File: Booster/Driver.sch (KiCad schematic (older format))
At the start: 5 parts

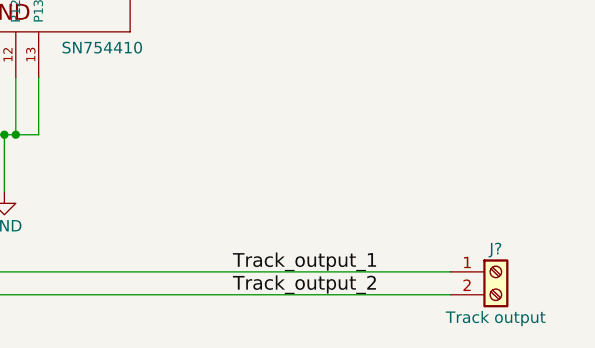
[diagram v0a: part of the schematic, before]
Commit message: First draft of detecting overcurrent.
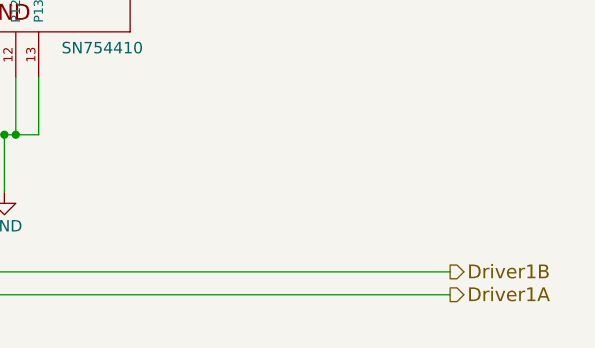
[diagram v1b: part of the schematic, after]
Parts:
- removed J?: Track output, symbol Screw_Terminal_01x02
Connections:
- net labels added: Driver1A, Driver1B
- net labels removed: Track_output_1, Track_output_2
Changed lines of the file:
@@
 $Descr A4 11693 8268
 encoding utf-8
-Sheet 4 4
+Sheet 4 5
 Title ""
 Date ""
@@
 Wire Wire Line
 	6500 5600 9150 5600
-$Comp
-L Screw_Terminal_01x02 J?
-U 1 1 59E91272
-P 9350 5500
-F 0 "J?" H 9350 5600 50  0000 C CNN
-F 1 "Track output" H 9350 5300 50  0000 C CNN
-F 2 "" H 9350 5500 50  0001 C CNN
-F 3 "" H 9350 5500 50  0001 C CNN
-	1    9350 5500
-	1    0    0    -1
-$EndComp
-Text Label 8200 5500 0    60   ~ 0
-Track_output_1
-Text Label 8200 5600 0    60   ~ 0
-Track_output_2
+Text HLabel 9150 5500 2    60   Output ~ 0
+Driver1B
+Text HLabel 9150 5600 2    60   Output ~ 0
+Driver1A
 $EndSCHEMATC

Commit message: Over current protection and detection - with detection delay and release delay.
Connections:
- net labels added: Enable_Driver, TrackA, TrackB, VCC_Driver
- net labels removed: +12V, DCC_Enable, Driver1A, Driver1B
- wire segments 29 -> 55
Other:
- moved on the sheet: C?
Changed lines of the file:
@@
-$EndComp
-$Comp
-L +12V #PWR?
-U 1 1 59E90E37
-P 7650 1900
-F 0 "#PWR?" H 7650 1750 50  0001 C CNN
-F 1 "+12V" H 7650 2040 50  0000 C CNN
-F 2 "" H 7650 1900 50  0001 C CNN
-F 3 "" H 7650 1900 50  0001 C CNN
-	1    7650 1900
-	1    0    0    -1
 $EndComp
 $Comp
 L C C?
 U 1 1 59E90E3D
-P 6950 2700
-F 0 "C?" H 6975 2800 50  0000 L CNN
-F 1 "100nF" H 6975 2600 50  0000 L CNN
-F 2 "" H 6988 2550 50  0001 C CNN
-F 3 "" H 6950 2700 50  0001 C CNN
-	1    6950 2700
+P 6950 2600
+F 0 "C?" H 6975 2700 50  0000 L CNN
+F 1 "100nF" H 6975 2500 50  0000 L CNN
+F 2 "" H 6988 2450 50  0001 C CNN
+F 3 "" H 6950 2600 50  0001 C CNN
+	1    6950 2600
 	1    0    0    -1
 $EndComp
@@
 L GND #PWR?
 U 1 1 59E90E44
-P 6950 3000
-F 0 "#PWR?" H 6950 2750 50  0001 C CNN
-F 1 "GND" H 6950 2850 50  0000 C CNN
-F 2 "" H 6950 3000 50  0001 C CNN
-F 3 "" H 6950 3000 50  0001 C CNN
-	1    6950 3000
+P 6950 2900
+F 0 "#PWR?" H 6950 2650 50  0001 C CNN
+F 1 "GND" H 6950 2750 50  0000 C CNN
+F 2 "" H 6950 2900 50  0001 C CNN
+F 3 "" H 6950 2900 50  0001 C CNN
+	1    6950 2900
 	1    0    0    -1
 $EndComp
@@
 L C C?
 U 1 1 59E90E4A
-P 7650 2700
-F 0 "C?" H 7675 2800 50  0000 L CNN
-F 1 "100nF" H 7675 2600 50  0000 L CNN
-F 2 "" H 7688 2550 50  0001 C CNN
-F 3 "" H 7650 2700 50  0001 C CNN
-	1    7650 2700
+P 7650 2600
+F 0 "C?" H 7675 2700 50  0000 L CNN
+F 1 "100nF" H 7675 2500 50  0000 L CNN
+F 2 "" H 7688 2450 50  0001 C CNN
+F 3 "" H 7650 2600 50  0001 C CNN
+	1    7650 2600
 	1    0    0    -1
 $EndComp
@@
 L GND #PWR?
 U 1 1 59E90E51
-P 7650 3000
-F 0 "#PWR?" H 7650 2750 50  0001 C CNN
-F 1 "GND" H 7650 2850 50  0000 C CNN
-F 2 "" H 7650 3000 50  0001 C CNN
-F 3 "" H 7650 3000 50  0001 C CNN
-	1    7650 3000
-	1    0    0    -1
-$EndComp
-Wire Wire Line
-	6950 1900 6950 2550
-Connection ~ 6950 2450
-Wire Wire Line
-	6950 3000 6950 2850
-Wire Wire Line
-	7650 3000 7650 2850
-Wire Wire Line
-	7650 1900 7650 2550
-Wire Wire Line
-	7650 2450 7350 2450
+P 7650 2900
+F 0 "#PWR?" H 7650 2650 50  0001 C CNN
+F 1 "GND" H 7650 2750 50  0000 C CNN
+F 2 "" H 7650 2900 50  0001 C CNN
+F 3 "" H 7650 2900 50  0001 C CNN
+	1    7650 2900
+	1    0    0    -1
+$EndComp
+Wire Wire Line
+	6950 1800 6950 2350
+Wire Wire Line
+	6950 2350 6950 2450
+Connection ~ 6950 2350
+Wire Wire Line
+	6950 2900 6950 2750
+Wire Wire Line
+	7650 2900 7650 2750
+Wire Wire Line
+	7650 1350 7650 2350
+Wire Wire Line
+	7650 2350 7650 2450
+Wire Wire Line
+	7650 2350 7350 2350
 $Comp
 L 74HC04 U?
@@
 	5900 3850 5900 4000
 Wire Wire Line
+	5900 4000 5900 5600
+Wire Wire Line
 	5900 3850 6650 3850
 Wire Wire Line
 	6650 3950 6350 3950
 Wire Wire Line
-	4550 3750 6650 3750
+	4550 3750 6300 3750
+Wire Wire Line
+	6300 3750 6650 3750
 Wire Wire Line
 	7050 4650 7050 4900
 Wire Wire Line
-	7050 4900 7350 4900
+	7050 4900 7150 4900
+Wire Wire Line
+	7150 4900 7200 4900
+Wire Wire Line
+	7200 4900 7250 4900
+Wire Wire Line
+	7250 4900 7350 4900
 Wire Wire Line
 	7200 4900 7200 5150
@@
 L +5V #PWR?
 U 1 1 59E90F12
-P 6950 1900
-F 0 "#PWR?" H 6950 1750 50  0001 C CNN
-F 1 "+5V" H 6950 2040 50  0000 C CNN
-F 2 "" H 6950 1900 50  0001 C CNN
-F 3 "" H 6950 1900 50  0001 C CNN
-	1    6950 1900
-	1    0    0    -1
-$EndComp
-Connection ~ 7650 2450
-Wire Wire Line
-	7350 2450 7350 3250
-Wire Wire Line
-	6950 2450 7250 2450
-Wire Wire Line
-	7250 2450 7250 3250
+P 6950 1800
+F 0 "#PWR?" H 6950 1650 50  0001 C CNN
+F 1 "+5V" H 6950 1940 50  0000 C CNN
+F 2 "" H 6950 1800 50  0001 C CNN
+F 3 "" H 6950 1800 50  0001 C CNN
+	1    6950 1800
+	1    0    0    -1
+$EndComp
+Connection ~ 7650 2350
+Wire Wire Line
+	7350 2350 7350 3250
+Wire Wire Line
+	6950 2350 7250 2350
+Wire Wire Line
+	7250 2350 7250 3250
 Text HLabel 4550 3750 0    60   Input ~ 0
-DCC_Enable
+Enable_Driver
 Text HLabel 4500 4350 0    60   Input ~ 0
 DCC
@@
 	5900 4000 5850 4000
 Wire Wire Line
-	4500 4350 6350 4350
+	4500 4350 4850 4350
+Wire Wire Line
+	4850 4350 6350 4350
 Wire Wire Line
 	4950 4000 4850 4000
 Wire Wire Line
 	4850 4000 4850 4350
+Wire Wire Line
+	4850 4350 4850 5500
 Connection ~ 4850 4350
 Wire Wire Line
@@
 	6650 4250 6600 4250
 Wire Wire Line
-	6600 4250 6600 5500
-Wire Wire Line
-	6600 5500 9150 5500
+	6600 4250 6600 5950
+Wire Wire Line
+	6600 5950 8000 5950
+Wire Wire Line
+	8000 5950 9150 5950
 Wire Wire Line
 	6650 4150 6500 4150
 Wire Wire Line
-	6500 4150 6500 5600
-Wire Wire Line
-	6500 5600 9150 5600
-Text HLabel 9150 5500 2    60   Output ~ 0
-Driver1B
-Text HLabel 9150 5600 2    60   Output ~ 0
-Driver1A
+	6500 4150 6500 6050
+Wire Wire Line
+	6500 6050 8100 6050
+Wire Wire Line
+	8100 6050 9150 6050
+Text HLabel 9150 5950 2    60   Output ~ 0
+TrackA
+Text HLabel 9150 6050 2    60   Output ~ 0
+TrackB
+Text HLabel 4700 1350 0    60   Input ~ 0
+VCC_Driver
+Wire Wire Line
+	7650 1350 4700 1350
+Wire Wire Line
+	4850 5500 8350 5500
+Wire Wire Line
+	8350 5500 8350 3950
+Wire Wire Line
+	8350 3950 7950 3950
+Wire Wire Line
+	6300 3750 6300 3200
+Wire Wire Line
+	6300 3200 8350 3200
+Wire Wire Line
+	8350 3200 8350 3750
+Wire Wire Line
+	8350 3750 7950 3750
+Connection ~ 6300 3750
+Wire Wire Line
+	5900 5600 8450 5600
+Wire Wire Line
+	8450 5600 8450 3850
+Wire Wire Line
+	8450 3850 7950 3850
+Connection ~ 5900 4000
+Wire Wire Line
+	7950 4250 8000 4250
+Wire Wire Line
+	8000 4250 8000 5950
+Connection ~ 8000 5950
+Wire Wire Line
+	7950 4150 8100 4150
+Wire Wire Line
+	8100 4150 8100 6050
+Connection ~ 8100 6050
 $EndSCHEMATC

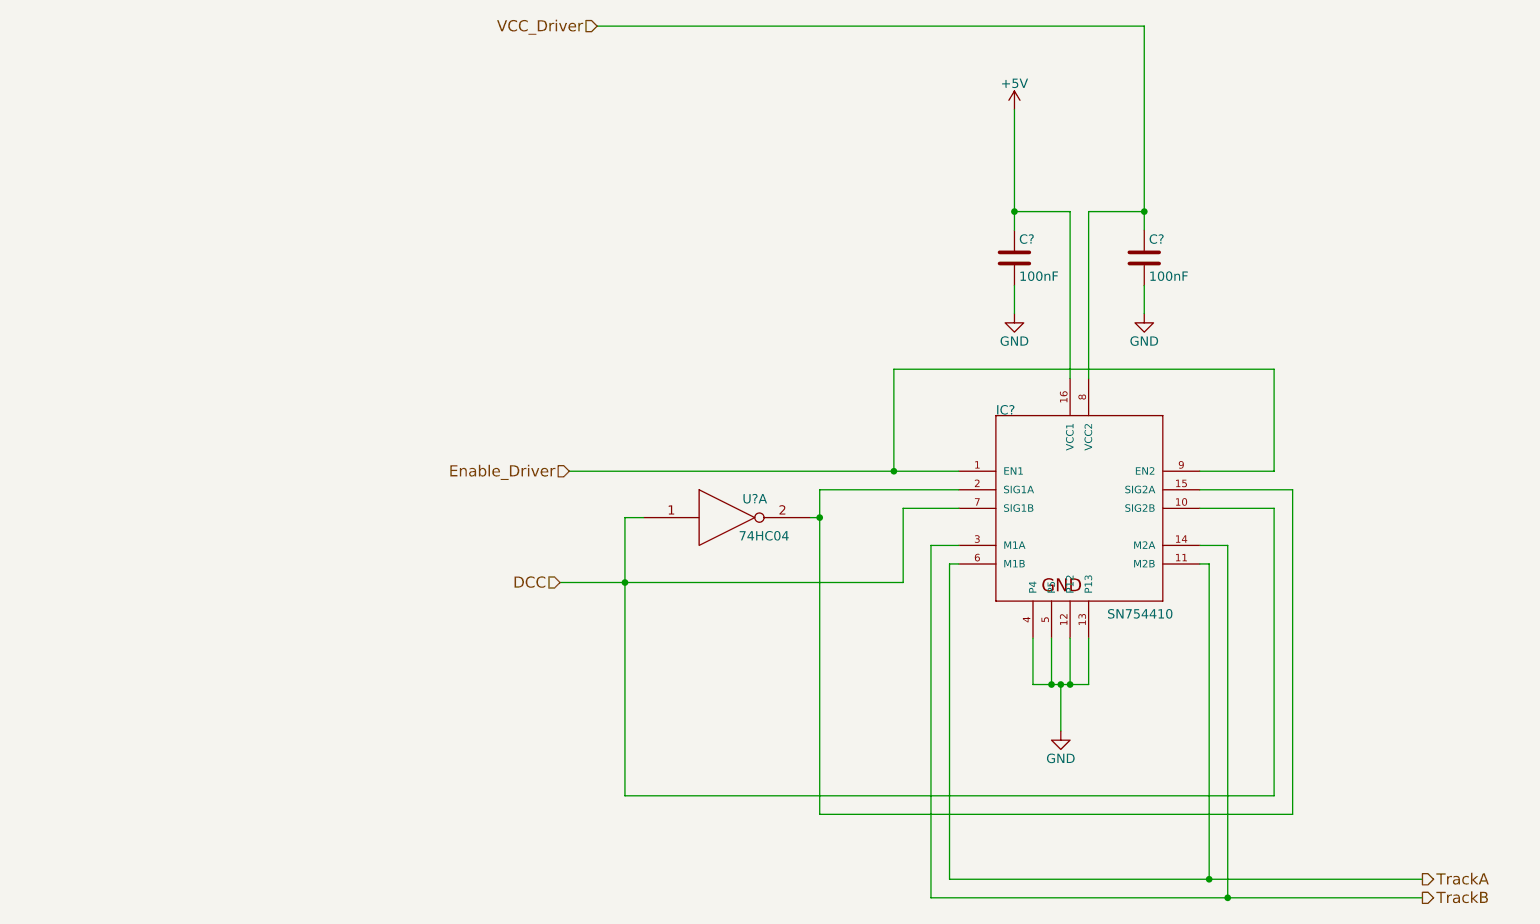
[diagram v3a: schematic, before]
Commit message: Added reversing support. Working on status output.
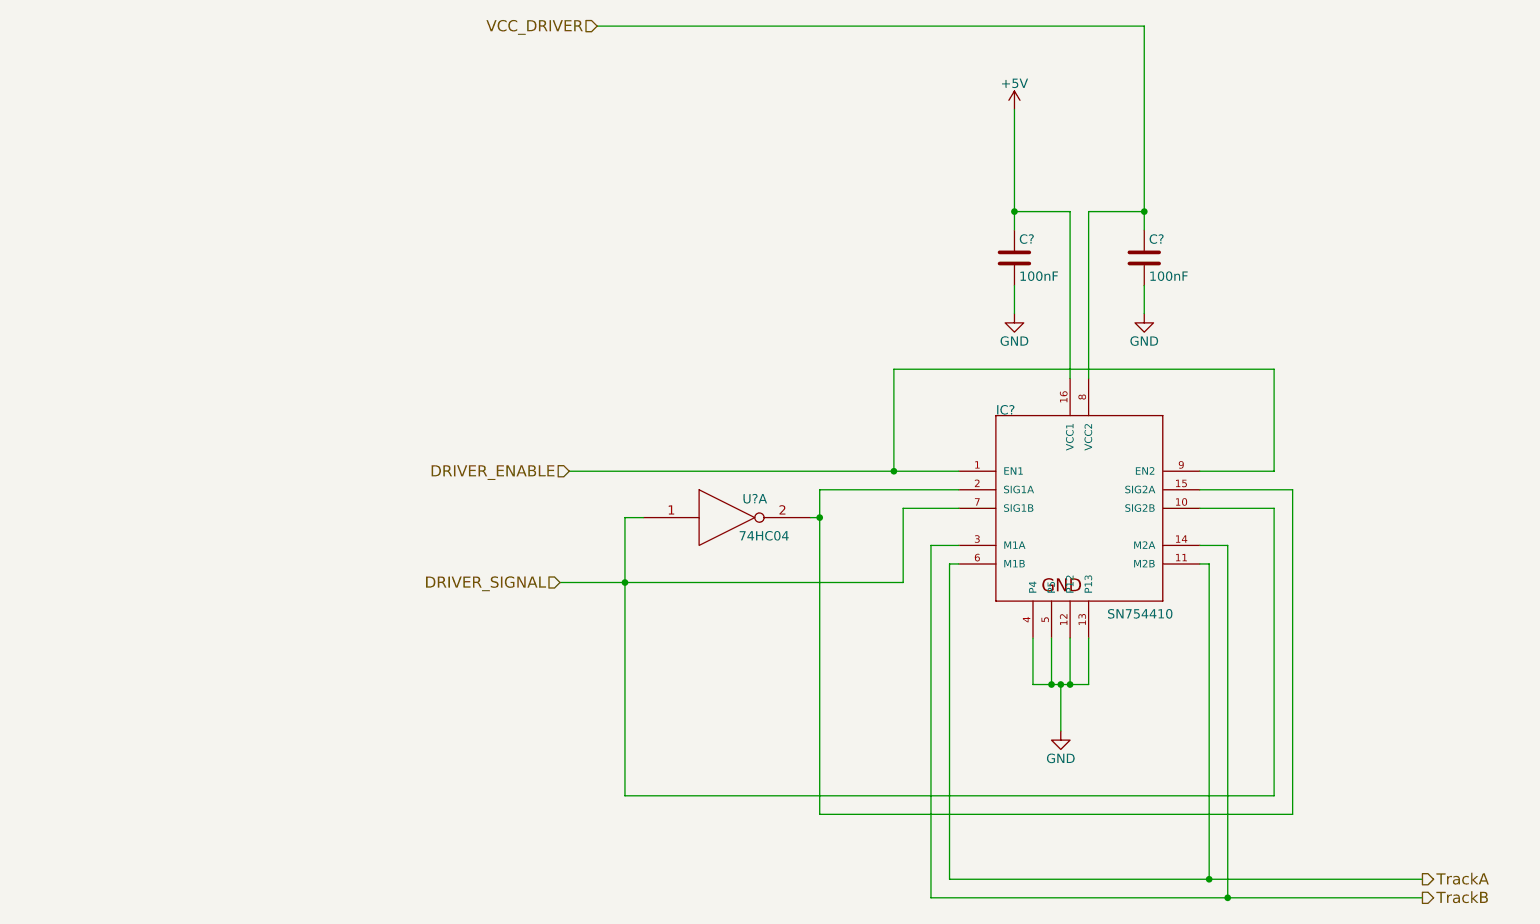
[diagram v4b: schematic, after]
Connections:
- net DCC renamed DRIVER_SIGNAL
- net Enable_Driver renamed DRIVER_ENABLE
- net VCC_Driver renamed VCC_DRIVER
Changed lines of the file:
@@
 $Descr A4 11693 8268
 encoding utf-8
-Sheet 4 6
+Sheet 4 7
 Title ""
 Date ""
@@
 $EndComp
 Wire Wire Line
-	6950 1800 6950 2350
-Wire Wire Line
-	6950 2350 6950 2450
+	6950 1800 6950 2450
 Connection ~ 6950 2350
 Wire Wire Line
@@
 	7650 2900 7650 2750
 Wire Wire Line
-	7650 1350 7650 2350
-Wire Wire Line
-	7650 2350 7650 2450
+	7650 1350 7650 2450
 Wire Wire Line
 	7650 2350 7350 2350
@@
 $EndComp
 Wire Wire Line
-	5900 3850 5900 4000
-Wire Wire Line
-	5900 4000 5900 5600
+	5900 3850 5900 5600
 Wire Wire Line
 	5900 3850 6650 3850
@@
 	6650 3950 6350 3950
 Wire Wire Line
-	4550 3750 6300 3750
-Wire Wire Line
-	6300 3750 6650 3750
+	4550 3750 6650 3750
 Wire Wire Line
 	7050 4650 7050 4900
 Wire Wire Line
-	7050 4900 7150 4900
-Wire Wire Line
-	7150 4900 7200 4900
-Wire Wire Line
-	7200 4900 7250 4900
-Wire Wire Line
-	7250 4900 7350 4900
+	7050 4900 7350 4900
 Wire Wire Line
 	7200 4900 7200 5150
@@
 	7250 2350 7250 3250
 Text HLabel 4550 3750 0    60   Input ~ 0
-Enable_Driver
+DRIVER_ENABLE
 Text HLabel 4500 4350 0    60   Input ~ 0
-DCC
+DRIVER_SIGNAL
 Wire Wire Line
 	5900 4000 5850 4000
 Wire Wire Line
-	4500 4350 4850 4350
-Wire Wire Line
-	4850 4350 6350 4350
+	4500 4350 6350 4350
 Wire Wire Line
 	4950 4000 4850 4000
 Wire Wire Line
-	4850 4000 4850 4350
-Wire Wire Line
-	4850 4350 4850 5500
+	4850 4000 4850 5500
 Connection ~ 4850 4350
 Wire Wire Line
@@
 	6600 4250 6600 5950
 Wire Wire Line
-	6600 5950 8000 5950
-Wire Wire Line
-	8000 5950 9150 5950
+	6600 5950 9150 5950
 Wire Wire Line
 	6650 4150 6500 4150
@@
 	6500 4150 6500 6050
 Wire Wire Line
-	6500 6050 8100 6050
-Wire Wire Line
-	8100 6050 9150 6050
+	6500 6050 9150 6050
 Text HLabel 9150 5950 2    60   Output ~ 0
 TrackA
@@
 TrackB
 Text HLabel 4700 1350 0    60   Input ~ 0
-VCC_Driver
+VCC_DRIVER
 Wire Wire Line
 	7650 1350 4700 1350

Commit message: Added meassurement tabs and other general "finalizing touches"
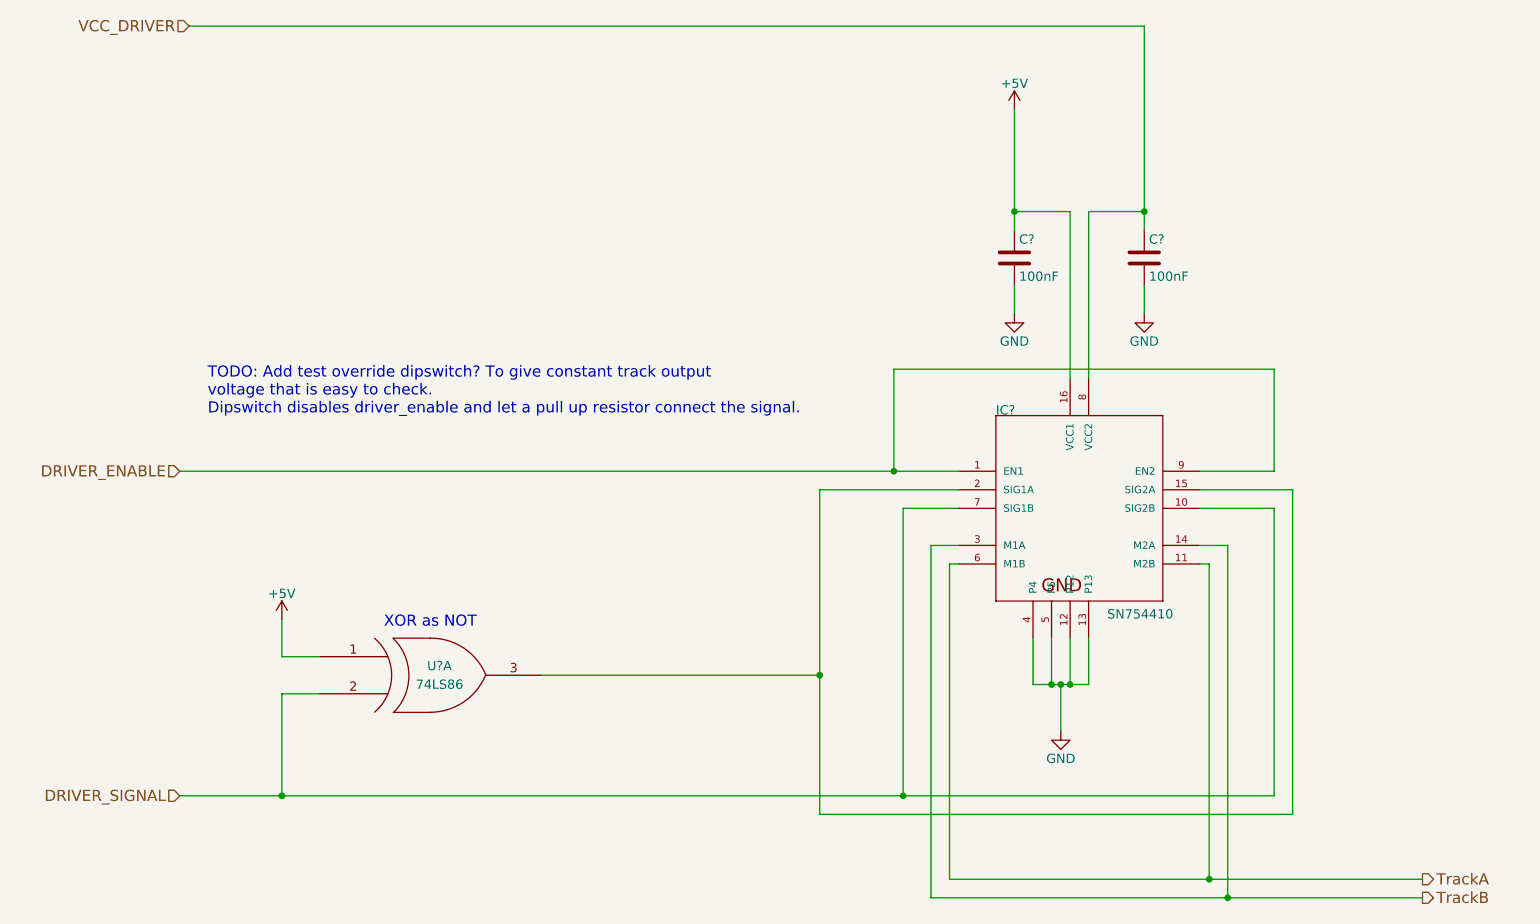
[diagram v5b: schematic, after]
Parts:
- removed U?: 74HC04, symbol 74HC04
- added U?: 74LS86, symbol 74LS86
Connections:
- net +5V: now also U?.1 (IN1)
- net DRIVER_SIGNAL: now also U?.2 (IN2)
- net GND: now also U?.7 (GND)
- net VCC: now also U?.14 (VCC)
- net at IC?.15 (SIG2A), IC?.2 (SIG1A): now also U?.3 (OUT)
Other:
- note added: "TODO: Add test override dipswitch? To give constant track output\nvoltage that is easy to check.\nDipswitch disables driver_enable and let a pull up resistor connect the signal."
- note added: "XOR as NOT"
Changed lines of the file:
@@
 Wire Wire Line
 	7650 2350 7350 2350
-$Comp
-L 74HC04 U?
-U 1 1 59E90E60
-P 5400 4000
-F 0 "U?" H 5550 4100 50  0000 C CNN
-F 1 "74HC04" H 5600 3900 50  0000 C CNN
-F 2 "" H 5400 4000 50  0001 C CNN
-F 3 "" H 5400 4000 50  0001 C CNN
-	1    5400 4000
-	1    0    0    -1
-$EndComp
 Wire Wire Line
 	5900 3850 5900 5600
@@
 	6650 3950 6350 3950
 Wire Wire Line
-	4550 3750 6650 3750
+	2450 3750 6650 3750
 Wire Wire Line
 	7050 4650 7050 4900
@@
 Wire Wire Line
 	7250 2350 7250 3250
-Text HLabel 4550 3750 0    60   Input ~ 0
+Text HLabel 2450 3750 0    60   Input ~ 0
 DRIVER_ENABLE
-Text HLabel 4500 4350 0    60   Input ~ 0
+Text HLabel 2450 5500 0    60   Input ~ 0
 DRIVER_SIGNAL
-Wire Wire Line
-	5900 4000 5850 4000
-Wire Wire Line
-	4500 4350 6350 4350
-Wire Wire Line
-	4950 4000 4850 4000
-Wire Wire Line
-	4850 4000 4850 5500
-Connection ~ 4850 4350
-Wire Wire Line
-	6350 4350 6350 3950
 Wire Wire Line
 	6650 4250 6600 4250
@@
 Text HLabel 9150 6050 2    60   Output ~ 0
 TrackB
-Text HLabel 4700 1350 0    60   Input ~ 0
+Text HLabel 2500 1350 0    60   Input ~ 0
 VCC_DRIVER
 Wire Wire Line
-	7650 1350 4700 1350
+	7650 1350 2500 1350
 Wire Wire Line
-	4850 5500 8350 5500
+	2450 5500 8350 5500
 Wire Wire Line
 	8350 5500 8350 3950
@@
 Wire Wire Line
 	8450 3850 7950 3850
-Connection ~ 5900 4000
 Wire Wire Line
 	7950 4250 8000 4250
@@
 	8100 4150 8100 6050
 Connection ~ 8100 6050
+$Comp
+L 74LS86 U?
+U 1 1 5A0F63C2
+P 3800 4850
+F 0 "U?" H 3850 4900 50  0000 C CNN
+F 1 "74LS86" H 3850 4800 50  0000 C CNN
+F 2 "" H 3800 4850 50  0001 C CNN
+F 3 "" H 3800 4850 50  0001 C CNN
+	1    3800 4850
+	1    0    0    -1
+$EndComp
+Connection ~ 6350 5500
+Wire Wire Line
+	3200 4950 3000 4950
+Wire Wire Line
+	3000 4950 3000 5500
+Connection ~ 3000 5500
+Wire Wire Line
+	3200 4750 3000 4750
+Wire Wire Line
+	3000 4750 3000 4550
+$Comp
+L +5V #PWR?
+U 1 1 5A0F6545
+P 3000 4550
+F 0 "#PWR?" H 3000 4400 50  0001 C CNN
+F 1 "+5V" H 3000 4690 50  0000 C CNN
+F 2 "" H 3000 4550 50  0001 C CNN
+F 3 "" H 3000 4550 50  0001 C CNN
+	1    3000 4550
+	1    0    0    -1
+$EndComp
+Wire Wire Line
+	4400 4850 5900 4850
+Connection ~ 5900 4850
+Wire Wire Line
+	6350 3950 6350 5500
+Text Notes 3550 4600 0    60   ~ 0
+XOR as NOT
+Text Notes 2600 3450 0    60   ~ 0
+TODO: Add test override dipswitch? To give constant track output\nvoltage that is easy to check.\nDipswitch disables driver_enable and let a pull up resistor connect the signal.
 $EndSCHEMATC
